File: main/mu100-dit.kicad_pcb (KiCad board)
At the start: 2 copper layers, 18 x 40 mm, 22 parts, among them J1 Conn_01x10_Female, J2 Conn_01x02_Male, U1 TOTX-177L, U2 AK4103A, U3 APX809S-46SR-7

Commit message: Clean up schematics and board drawings
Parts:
- C1, C2, C3, C4: value 0.1u/35V -> 0.1uF
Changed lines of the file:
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@@
       (effects (font (size 1 1) (thickness 0.15)))
     )
-    (fp_text value "0.1u/35V" (at 0 1.68) (layer "F.Fab")
+    (fp_text value "0.1uF" (at 0 1.68) (layer "F.Fab")
       (effects (font (size 1 1) (thickness 0.15)))
     )
@@
       (effects (font (size 1 1) (thickness 0.15)))
     )
-    (fp_text value "0.1u/35V" (at 0 1.68) (layer "F.Fab")
+    (fp_text value "0.1uF" (at 0 1.68) (layer "F.Fab")
       (effects (font (size 1 1) (thickness 0.15)))
     )
@@
     (fp_line (start -0.7 -0.95) (end -0.15 -1.52) (layer "F.Fab") (width 0.1))
     (pad "1" smd rect (at -1.5 -0.95) (size 1.9 0.8) (layers "F.Cu" "F.Paste" "F.Mask")
-      (net 5 "/RESET") (pinfunction "*RESET") (pintype "output"))
+      (net 5 "/RESET") (pinfunction "~{RESET}") (pintype "output"))
     (pad "2" smd rect (at -1.5 0.95) (size 1.9 0.8) (layers "F.Cu" "F.Paste" "F.Mask")
       (net 1 "GND") (pinfunction "GND") (pintype "power_in"))
@@
       (effects (font (size 1 1) (thickness 0.15)))
     )
-    (fp_text value "0.1u/35V" (at 0 1.68) (layer "F.Fab")
+    (fp_text value "0.1uF" (at 0 1.68) (layer "F.Fab")
       (effects (font (size 1 1) (thickness 0.15)))
     )
@@
       (effects (font (size 1 1) (thickness 0.15)))
     )
-    (fp_text value "0.1u/35V" (at 0 1.68 180) (layer "F.Fab")
-      (effects (font (size 1 1) (thickness 0.15)))
-    )
+    (fp_text value "0.1uF" (at 0 1.68 180) (layer "F.Fab")
+      (effects (font (size 1 1) (thickness 0.15)))
+    )

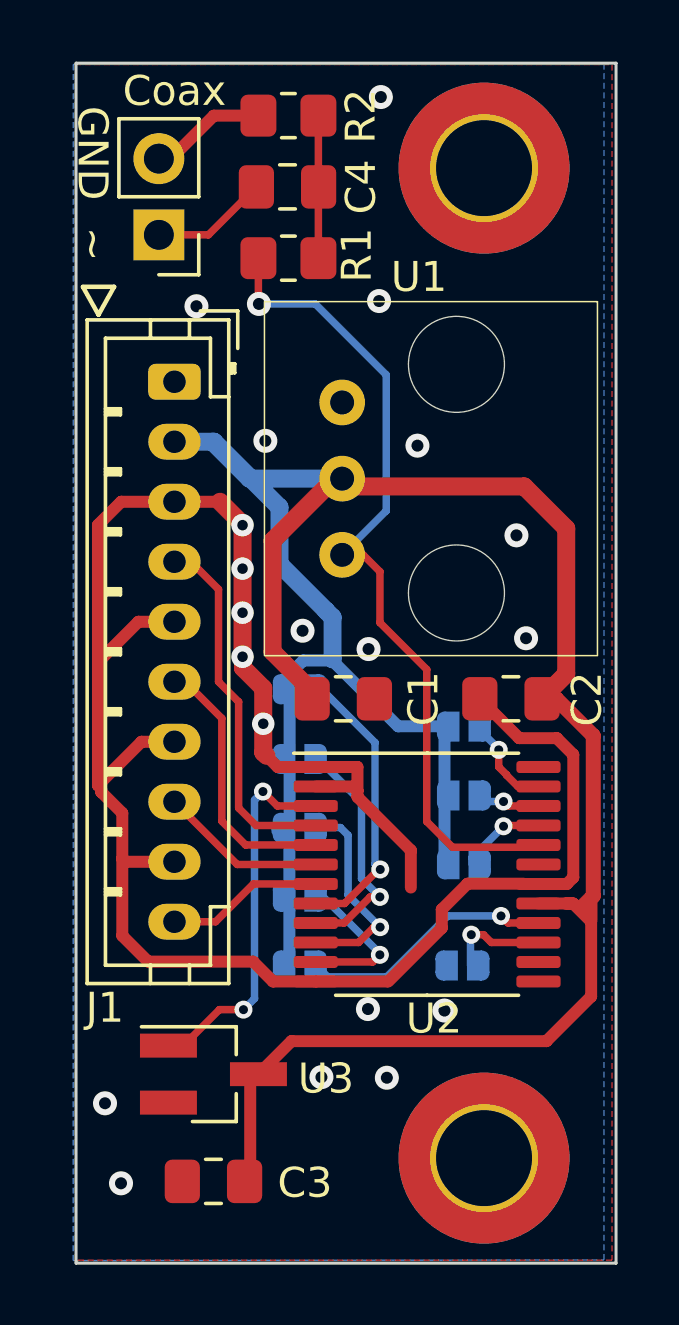
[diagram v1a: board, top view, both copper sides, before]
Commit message: Unground mounting holes, rearrange DIF0/DIF1 vias to avoid bridge
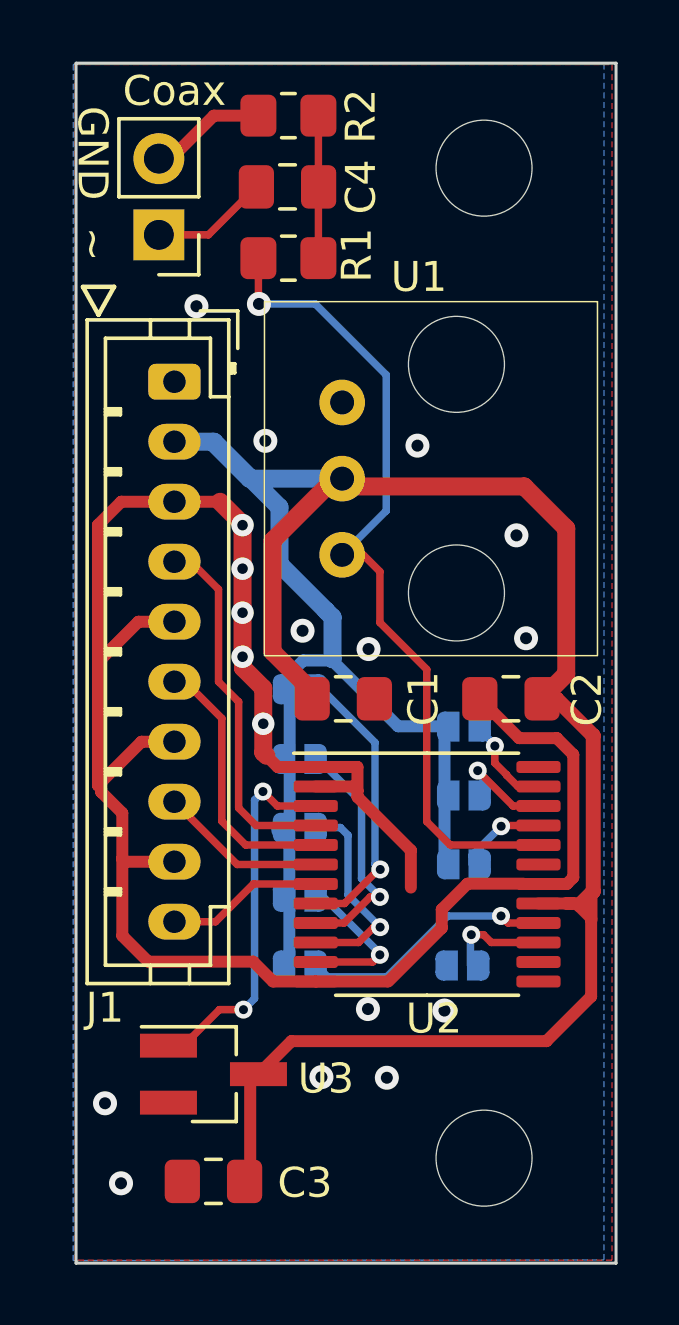
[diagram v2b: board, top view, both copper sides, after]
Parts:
- H1, H2: footprint MountingHole:MountingHole_3.2mm_M3_ISO7380_Pad_TopBottom -> MountingHole:MountingHole_3.2mm_M3_ISO7380
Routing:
- net /DIF1: track 1.99 -> 3.41 mm
- net GND: vias 20 -> 18

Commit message: minor tweaks to main board
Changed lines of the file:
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@@
   )
   (segment (start 82.55 94.572) (end 83.3 95.322) (width 0.6) (layer "F.Cu") (net 1))
-  (segment (start 92.5205 102.452) (end 91.2085 101.14) (width 0.4) (layer "F.Cu") (net 1))
   (segment (start 83.3 95.352) (end 83.3 99.7386) (width 0.6) (layer "F.Cu") (net 1))
   (segment (start 83.655 109.902) (end 80.155 109.902) (width 0.4) (layer "F.Cu") (net 1))
+  (segment (start 94.32548 107.09652) (end 94.32548 103.00248) (width 0.4) (layer "F.Cu") (net 1))
   (segment (start 86.991427 104.063427) (end 87.13 104.202) (width 0.4) (layer "F.Cu") (net 1))
+  (segment (start 93.1645 107.313427) (end 94.108573 107.313427) (width 0.4) (layer "F.Cu") (net 1))
   (segment (start 88.118573 110.563427) (end 85.7395 110.563427) (width 0.4) (layer "F.Cu") (net 1))
   (segment (start 85.7395 103.413427) (end 87.13 103.413427) (width 0.4) (layer "F.Cu") (net 1))
   (segment (start 78.588 104.246) (end 79.292 104.95) (width 0.4) (layer "F.Cu") (net 1))
   (segment (start 89.94 108.78) (end 89.94 108.162) (width 0.4) (layer "F.Cu") (net 1))
-  (segment (start 93.775 102.452) (end 92.5205 102.452) (width 0.4) (layer "F.Cu") (net 1))
   (segment (start 81.03 98.572) (end 79.828 98.572) (width 0.4) (layer "F.Cu") (net 1))
   (segment (start 78.48 99.92) (end 78.48 104.022) (width 0.4) (layer "F.Cu") (net 1))
@@
   (segment (start 83.99 101.972) (end 83.99 100.78601) (width 0.6) (layer "F.Cu") (net 1))
   (segment (start 79.292 109.039) (end 79.292 106.474) (width 0.4) (layer "F.Cu") (net 1))
-  (segment (start 94.32548 107.09652) (end 94.32548 103.00248) (width 0.4) (layer "F.Cu") (net 1))
   (segment (start 83.99 102.9306) (end 83.99 101.972) (width 0.6) (layer "F.Cu") (net 1))
   (segment (start 83.99 100.78601) (end 83.3126 100.10861) (width 0.6) (layer "F.Cu") (net 1))
   (segment (start 88.156573 110.563427) (end 89.94 108.78) (width 0.4) (layer "F.Cu") (net 1))
-  (segment (start 94.32548 103.00248) (end 93.775 102.452) (width 0.4) (layer "F.Cu") (net 1))
   (segment (start 81.03 94.572) (end 79.256 94.572) (width 0.4) (layer "F.Cu") (net 1))
   (segment (start 81.03 94.572) (end 82.55 94.572) (width 0.4) (layer "F.Cu") (net 1))
@@
   (segment (start 84.1 103.0406) (end 83.99 102.9306) (width 0.6) (layer "F.Cu") (net 1))
   (segment (start 85.7395 110.563427) (end 84.316427 110.563427) (width 0.4) (layer "F.Cu") (net 1))
+  (segment (start 94.32548 103.00248) (end 93.775 102.452) (width 0.4) (layer "F.Cu") (net 1))
+  (segment (start 94.108573 107.313427) (end 94.32548 107.09652) (width 0.4) (layer "F.Cu") (net 1))
   (segment (start 85.7395 104.063427) (end 86.991427 104.063427) (width 0.4) (layer "F.Cu") (net 1))
-  (segment (start 94.108573 107.313427) (end 94.32548 107.09652) (width 0.4) (layer "F.Cu") (net 1))
+  (segment (start 92.64 102.452) (end 91.328 101.14) (width 0.4) (layer "F.Cu") (net 1))
   (segment (start 78.48 104.022) (end 78.588 104.13) (width 0.4) (layer "F.Cu") (net 1))
   (segment (start 87.13 104.412) (end 88.91 106.192) (width 0.4) (layer "F.Cu") (net 1))
@@
   (segment (start 83.3126 100.10861) (end 83.3126 99.7132) (width 0.6) (layer "F.Cu") (net 1))
   (segment (start 87.13 104.202) (end 87.13 104.412) (width 0.4) (layer "F.Cu") (net 1))
+  (segment (start 91.328 101.14) (end 91.2085 101.14) (width 0.4) (layer "F.Cu") (net 1))
   (segment (start 79.292 104.95) (end 79.292 106.474) (width 0.4) (layer "F.Cu") (net 1))
   (segment (start 82.343 81.702) (end 80.91 83.135) (width 0.4) (layer "F.Cu") (net 1))
+  (segment (start 93.775 102.452) (end 92.64 102.452) (width 0.4) (layer "F.Cu") (net 1))
   (segment (start 80.155 109.902) (end 79.292 109.039) (width 0.4) (layer "F.Cu") (net 1))
   (segment (start 79.93 102.572) (end 78.48 104.022) (width 0.4) (layer "F.Cu") (net 1))
   (segment (start 78.48 95.348) (end 78.48 99.92) (width 0.4) (layer "F.Cu") (net 1))
   (segment (start 83.3 95.322) (end 83.3 95.352) (width 0.6) (layer "F.Cu") (net 1))
-  (segment (start 93.1645 107.313427) (end 94.108573 107.313427) (width 0.4) (layer "F.Cu") (net 1))
   (segment (start 87.13 103.413427) (end 87.13 104.202) (width 0.4) (layer "F.Cu") (net 1))
   (segment (start 89.94 108.162) (end 90.798573 107.303427) (width 0.4) (layer "F.Cu") (net 1))
@@
   (segment (start 91.138872 103.534614) (end 91.32 103.715742) (width 0.25) (layer "B.Cu") (net 14))
   (segment (start 91.32 103.715742) (end 91.32 104.352) (width 0.25) (layer "B.Cu") (net 14))
-  (segment (start 91.71 102.712) (end 91.71 103.282) (width 0.25) (layer "F.Cu") (net 15))
-  (segment (start 91.71 103.282) (end 92.10248 103.67448) (width 0.25) (layer "F.Cu") (net 15))
   (segment (start 92.10248 103.689268) (end 92.476639 104.063427) (width 0.25) (layer "F.Cu") (net 15))
-  (segment (start 92.10248 103.67448) (end 92.10248 103.689268) (width 0.25) (layer "F.Cu") (net 15))
+  (segment (start 92.10248 103.05448) (end 92.10248 103.689268) (width 0.25) (layer "F.Cu") (net 15))
+  (segment (start 91.75 102.702) (end 92.10248 103.05448) (width 0.25) (layer "F.Cu") (net 15))
   (segment (start 92.476639 104.063427) (end 93.1645 104.063427) (width 0.25) (layer "F.Cu") (net 15))
-  (via (at 91.71 102.712) (size 0.6) (drill 0.3) (layers "F.Cu" "B.Cu") (free) (net 15))
-  (segment (start 91.71 102.712) (end 91.71 102.682) (width 0.25) (layer "B.Cu") (net 15))
-  (segment (start 91.71 102.682) (end 91.085 102.057) (width 0.25) (layer "B.Cu") (net 15))
+  (via (at 91.75 102.702) (size 0.6) (drill 0.3) (layers "F.Cu" "B.Cu") (free) (net 15))
+  (segment (start 91.73 102.702) (end 91.085 102.057) (width 0.25) (layer "B.Cu") (net 15))
+  (segment (start 91.75 102.702) (end 91.73 102.702) (width 0.25) (layer "B.Cu") (net 15))
   (segment (start 91.3315 109.0035) (end 91.591427 109.263427) (width 0.25) (layer "F.Cu") (net 16))
   (segment (start 90.9252 109.0035) (end 91.3315 109.0035) (width 0.25) (layer "F.Cu") (net 16))
